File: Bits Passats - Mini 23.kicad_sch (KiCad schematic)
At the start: 0 parts

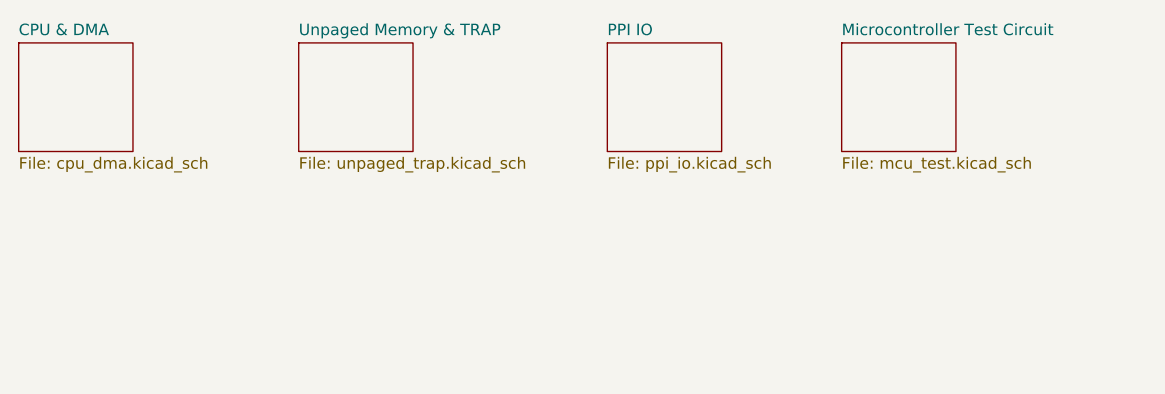
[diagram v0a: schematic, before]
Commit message: Updated to version 8
Changed to version 8; added 96-pin connectors; described ports at PPI_Settings
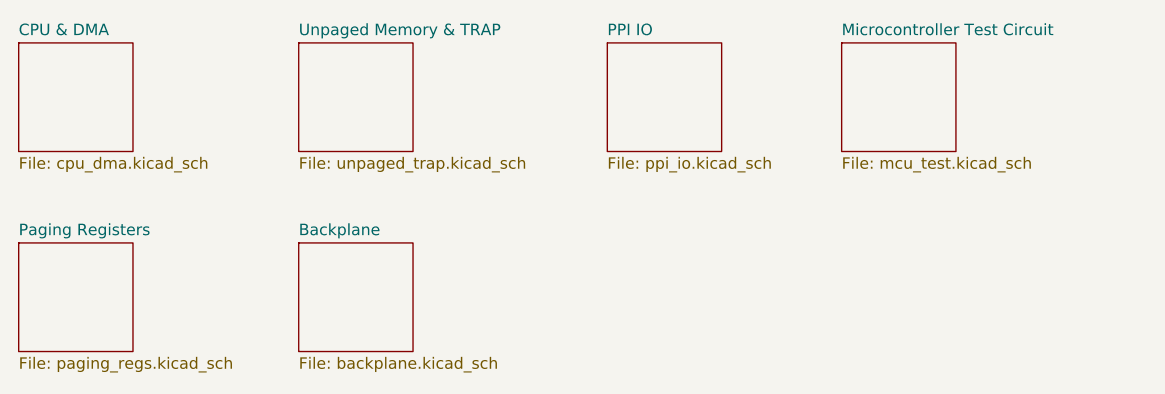
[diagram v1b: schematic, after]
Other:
- added sheet Backplane (backplane.kicad_sch)
- added sheet Paging Registers (paging_regs.kicad_sch)
